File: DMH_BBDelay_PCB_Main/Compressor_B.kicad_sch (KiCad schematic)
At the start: 23 parts, among them U27 SSI2162, U28 TL074

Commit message: Added notes from troubleshooting
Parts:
- C91: now not fitted
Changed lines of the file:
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@@
 		(on_board yes)
 		(in_pos_files yes)
-		(dnp no)
+		(dnp yes)
 		(property "Reference" "C91"
 			(at 50.8 134.62 0)

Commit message: Scaled up components in Tone Control part
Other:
- note added: "Bypassing this capacitor with a short improved the frequent loud excursions of this compressor."
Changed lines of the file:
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@@
 		(comment 1 "PCB for 10cm Kosmo format synthesizer module")
+	)
+	(text "Bypassing this capacitor with a short improved the frequent\nloud excursions of this compressor."
+		(exclude_from_sim no)
+		(at 91.694 133.858 0)
+		(effects
+			(font
+				(size 1.27 1.27)
+			)
+		)
 	)
 	(junction

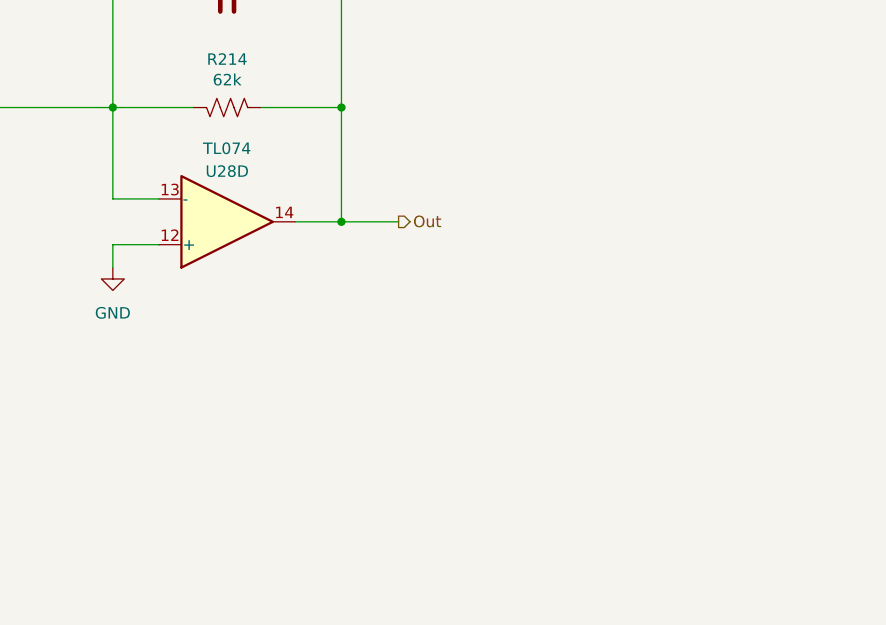
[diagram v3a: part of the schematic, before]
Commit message: Added clamping to compressors outputs
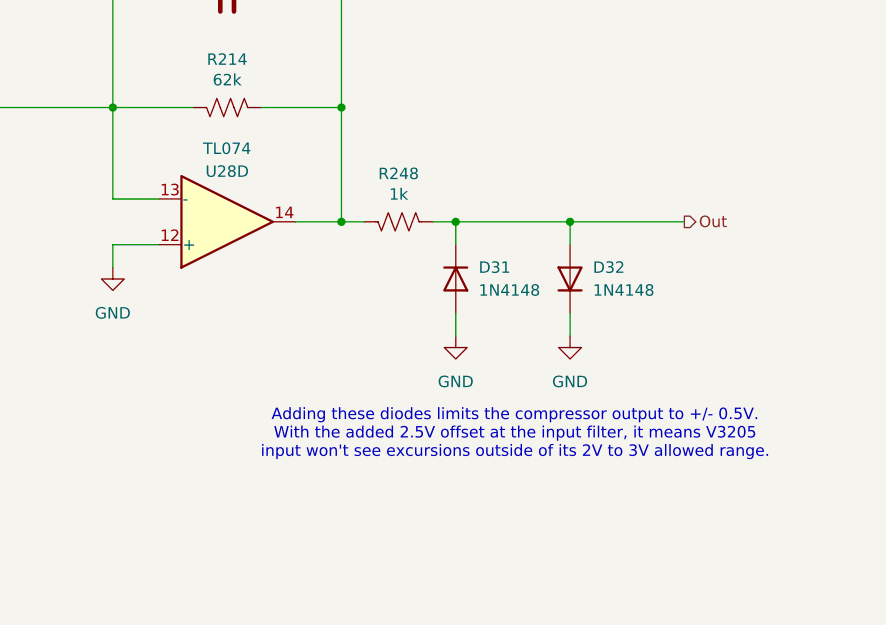
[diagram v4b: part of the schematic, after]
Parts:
- added D31, D32: 1N4148, Diode_THT:D_DO-35_SOD27_P7.62mm_Horizontal, symbol Diode:1N4148
- added R248: 1k, Resistor_THT:R_Axial_DIN0207_L6.3mm_D2.5mm_P7.62mm_Horizontal, symbol Device:R_US
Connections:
- net GND: now also D31.2 (A), D32.1 (K)
- net Out: now also D31.1 (K), D32.2 (A), R248.2; no longer C97.2, R214.2, R215.1, U28.14
- new net: C97.2, R214.2, R215.1, R248.1, U28.14
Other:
- note added: "Adding these diodes limits the compressor output to +/- 0.5V. With the added 2.5V offset at the input filter, it means V3205 input won't see excursions outside of its 2V to 3V allowed range."
